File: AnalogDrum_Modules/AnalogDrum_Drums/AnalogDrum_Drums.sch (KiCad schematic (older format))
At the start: 11 parts, among them J101 Conn_01x05_Male, SW101 SW_SPDT

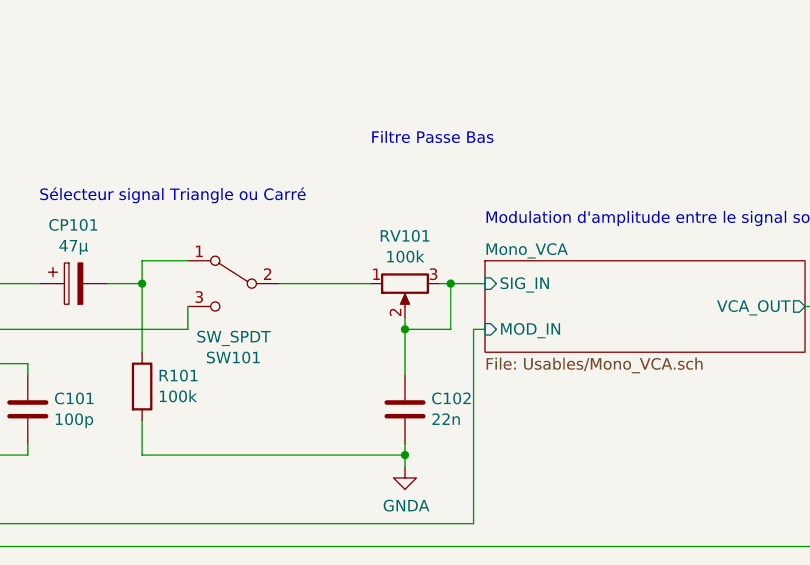
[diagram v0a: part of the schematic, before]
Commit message: Version 0.1.1
Corrections mineures :
- Vérification des potentiomètres
- Passage des connecteurs de carte e n JST
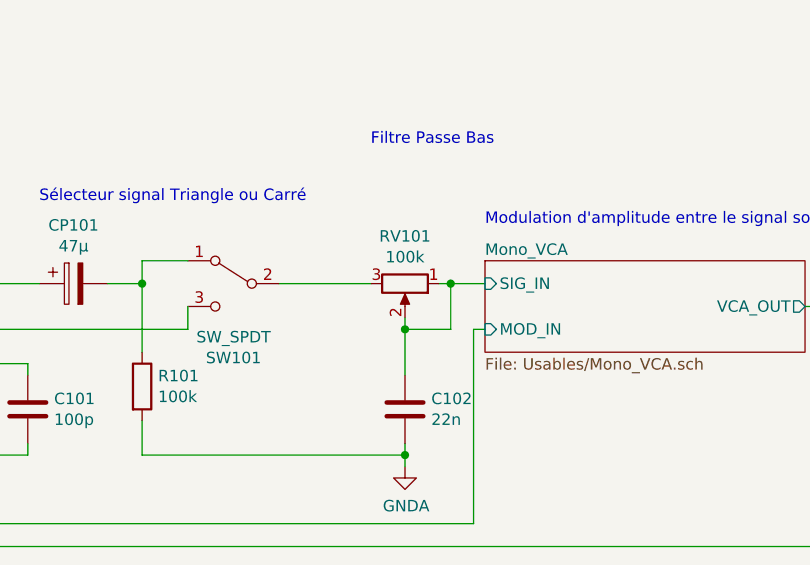
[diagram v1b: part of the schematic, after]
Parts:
- J101: footprint Connector_PinHeader_2.54mm:PinHeader_1x05_P2.54mm_Horizontal -> Connector_JST:JST_EH_B5B-EH-A_1x05_P2.50mm_Vertical
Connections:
- net Mono_VCA/SIG_IN: now also RV101.1; no longer RV101.3
- net at SW101.2 (B): now also RV101.3; no longer RV101.1
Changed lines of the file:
@@
 F 3 "~" H 7800 3150 50  0001 C CNN
 	1    7800 3150
-	0    -1   1    0
+	0    1    1    0
 $EndComp
 Wire Wire Line
@@
 F 0 "J101" H 2458 3831 50  0000 C CNN
 F 1 "Conn_01x05_Male" H 2458 3740 50  0000 C CNN
-F 2 "Connector_PinHeader_2.54mm:PinHeader_1x05_P2.54mm_Horizontal" H 2350 3450 50  0001 C CNN
+F 2 "Connector_JST:JST_EH_B5B-EH-A_1x05_P2.50mm_Vertical" H 2350 3450 50  0001 C CNN
 F 3 "~" H 2350 3450 50  0001 C CNN
 	1    2350 3450
